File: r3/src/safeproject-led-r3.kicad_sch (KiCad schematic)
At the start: 22 parts, among them J201 2314844-8, J202 FH12A-20S-0.5SH

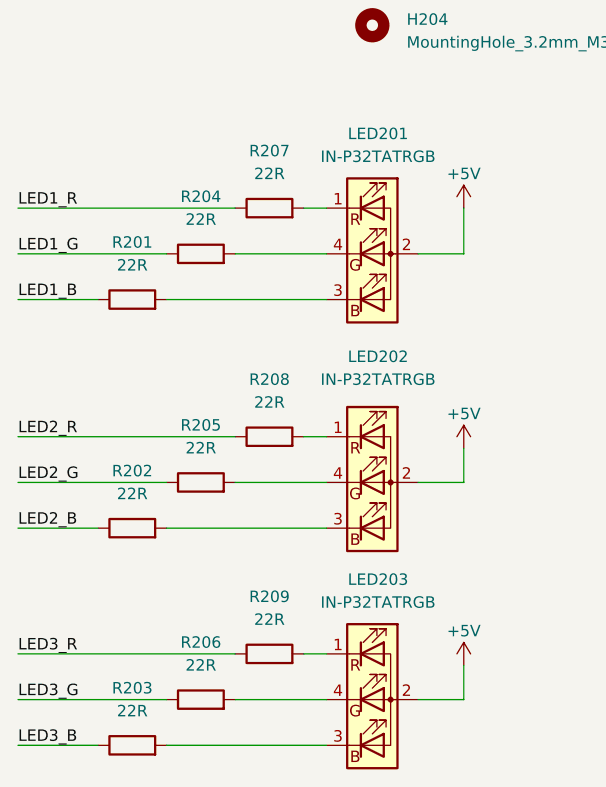
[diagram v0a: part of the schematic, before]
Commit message: Change resistor values to dim LED's way down
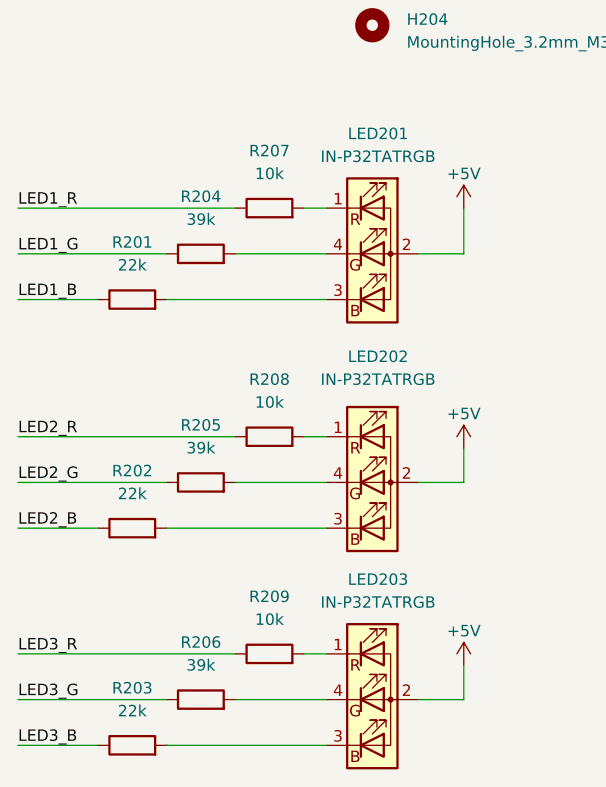
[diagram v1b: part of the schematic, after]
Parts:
- R201, R202, R203: value 22R -> 22k
- R204, R205, R206: value 22R -> 39k
- R207, R208, R209: value 22R -> 10k
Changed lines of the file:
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@@
     (in_bom yes) (on_board yes)
     (property "Reference" "R201" (id 0) (at 87.63 73.66 90))
-    (property "Value" "22R" (id 1) (at 87.63 76.2 90))
+    (property "Value" "22k" (id 1) (at 87.63 76.2 90))
     (property "Footprint" "Resistor_SMD:R_0603_1608Metric" (id 2) (at 87.63 81.788 90)
       (effects (font (size 1.27 1.27)) hide)
@@
     (in_bom yes) (on_board yes)
     (property "Reference" "R202" (id 0) (at 87.63 99.06 90))
-    (property "Value" "22R" (id 1) (at 87.63 101.6 90))
+    (property "Value" "22k" (id 1) (at 87.63 101.6 90))
     (property "Footprint" "Resistor_SMD:R_0603_1608Metric" (id 2) (at 87.63 107.188 90)
       (effects (font (size 1.27 1.27)) hide)
@@
     (in_bom yes) (on_board yes)
     (property "Reference" "R203" (id 0) (at 87.63 123.19 90))
-    (property "Value" "22R" (id 1) (at 87.63 125.73 90))
+    (property "Value" "22k" (id 1) (at 87.63 125.73 90))
     (property "Footprint" "Resistor_SMD:R_0603_1608Metric" (id 2) (at 87.63 131.318 90)
       (effects (font (size 1.27 1.27)) hide)
@@
     (in_bom yes) (on_board yes)
     (property "Reference" "R204" (id 0) (at 95.25 68.58 90))
-    (property "Value" "22R" (id 1) (at 95.25 71.12 90))
+    (property "Value" "39k" (id 1) (at 95.25 71.12 90))
     (property "Footprint" "Resistor_SMD:R_0603_1608Metric" (id 2) (at 95.25 76.708 90)
       (effects (font (size 1.27 1.27)) hide)
@@
     (in_bom yes) (on_board yes)
     (property "Reference" "R205" (id 0) (at 95.25 93.98 90))
-    (property "Value" "22R" (id 1) (at 95.25 96.52 90))
+    (property "Value" "39k" (id 1) (at 95.25 96.52 90))
     (property "Footprint" "Resistor_SMD:R_0603_1608Metric" (id 2) (at 95.25 102.108 90)
       (effects (font (size 1.27 1.27)) hide)
@@
     (in_bom yes) (on_board yes)
     (property "Reference" "R206" (id 0) (at 95.25 118.11 90))
-    (property "Value" "22R" (id 1) (at 95.25 120.65 90))
+    (property "Value" "39k" (id 1) (at 95.25 120.65 90))
     (property "Footprint" "Resistor_SMD:R_0603_1608Metric" (id 2) (at 95.25 126.238 90)
       (effects (font (size 1.27 1.27)) hide)
@@
     (in_bom yes) (on_board yes)
     (property "Reference" "R207" (id 0) (at 102.87 63.5 90))
-    (property "Value" "22R" (id 1) (at 102.87 66.04 90))
+    (property "Value" "10k" (id 1) (at 102.87 66.04 90))
     (property "Footprint" "Resistor_SMD:R_0603_1608Metric" (id 2) (at 102.87 71.628 90)
       (effects (font (size 1.27 1.27)) hide)
@@
     (in_bom yes) (on_board yes)
     (property "Reference" "R208" (id 0) (at 102.87 88.9 90))
-    (property "Value" "22R" (id 1) (at 102.87 91.44 90))
+    (property "Value" "10k" (id 1) (at 102.87 91.44 90))
     (property "Footprint" "Resistor_SMD:R_0603_1608Metric" (id 2) (at 102.87 97.028 90)
       (effects (font (size 1.27 1.27)) hide)
@@
     (in_bom yes) (on_board yes)
     (property "Reference" "R209" (id 0) (at 102.87 113.03 90))
-    (property "Value" "22R" (id 1) (at 102.87 115.57 90))
+    (property "Value" "10k" (id 1) (at 102.87 115.57 90))
     (property "Footprint" "Resistor_SMD:R_0603_1608Metric" (id 2) (at 102.87 121.158 90)
       (effects (font (size 1.27 1.27)) hide)
@@
     )
     (path "/cb9ccd1a-13ee-4624-9a4b-802e65d85af0"
-      (reference "R201") (unit 1) (value "22R") (footprint "Resistor_SMD:R_0603_1608Metric")
+      (reference "R201") (unit 1) (value "22k") (footprint "Resistor_SMD:R_0603_1608Metric")
     )
     (path "/58417487-3113-430b-9fc9-009d58e12415"
-      (reference "R202") (unit 1) (value "22R") (footprint "Resistor_SMD:R_0603_1608Metric")
+      (reference "R202") (unit 1) (value "22k") (footprint "Resistor_SMD:R_0603_1608Metric")
     )
     (path "/69397af2-1fee-4dec-9a03-ceb5f4e62e36"
-      (reference "R203") (unit 1) (value "22R") (footprint "Resistor_SMD:R_0603_1608Metric")
+      (reference "R203") (unit 1) (value "22k") (footprint "Resistor_SMD:R_0603_1608Metric")
     )
     (path "/c524c284-9623-4d8f-8e53-21acea5f02d2"
-      (reference "R204") (unit 1) (value "22R") (footprint "Resistor_SMD:R_0603_1608Metric")
+      (reference "R204") (unit 1) (value "39k") (footprint "Resistor_SMD:R_0603_1608Metric")
     )
     (path "/a7e2b58d-ba9e-4fb3-b19a-297697c34f7b"
-      (reference "R205") (unit 1) (value "22R") (footprint "Resistor_SMD:R_0603_1608Metric")
+      (reference "R205") (unit 1) (value "39k") (footprint "Resistor_SMD:R_0603_1608Metric")
     )
     (path "/c6476391-e7ce-4809-8a1f-47e170294b69"
-      (reference "R206") (unit 1) (value "22R") (footprint "Resistor_SMD:R_0603_1608Metric")
+      (reference "R206") (unit 1) (value "39k") (footprint "Resistor_SMD:R_0603_1608Metric")
     )
     (path "/37846301-7f60-44b4-9487-f411f7747188"
-      (reference "R207") (unit 1) (value "22R") (footprint "Resistor_SMD:R_0603_1608Metric")
+      (reference "R207") (unit 1) (value "10k") (footprint "Resistor_SMD:R_0603_1608Metric")
     )
     (path "/a87c8174-14da-4d1e-9d88-2fc40c19646c"
-      (reference "R208") (unit 1) (value "22R") (footprint "Resistor_SMD:R_0603_1608Metric")
+      (reference "R208") (unit 1) (value "10k") (footprint "Resistor_SMD:R_0603_1608Metric")
     )
     (path "/88245093-eea4-4fee-985c-b7064722ebde"
-      (reference "R209") (unit 1) (value "22R") (footprint "Resistor_SMD:R_0603_1608Metric")
-    )
-  )
+      (reference "R209") (unit 1) (value "10k") (footprint "Resistor_SMD:R_0603_1608Metric")
+    )
+  )
